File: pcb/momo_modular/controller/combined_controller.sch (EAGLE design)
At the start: 48 parts, among them Q2 P-MOSFET, U1 XRP7659, U2 PIC24FJ64GA306, U3 MCP1702, U5 FLASH8MSOP8, U6 MCP73811

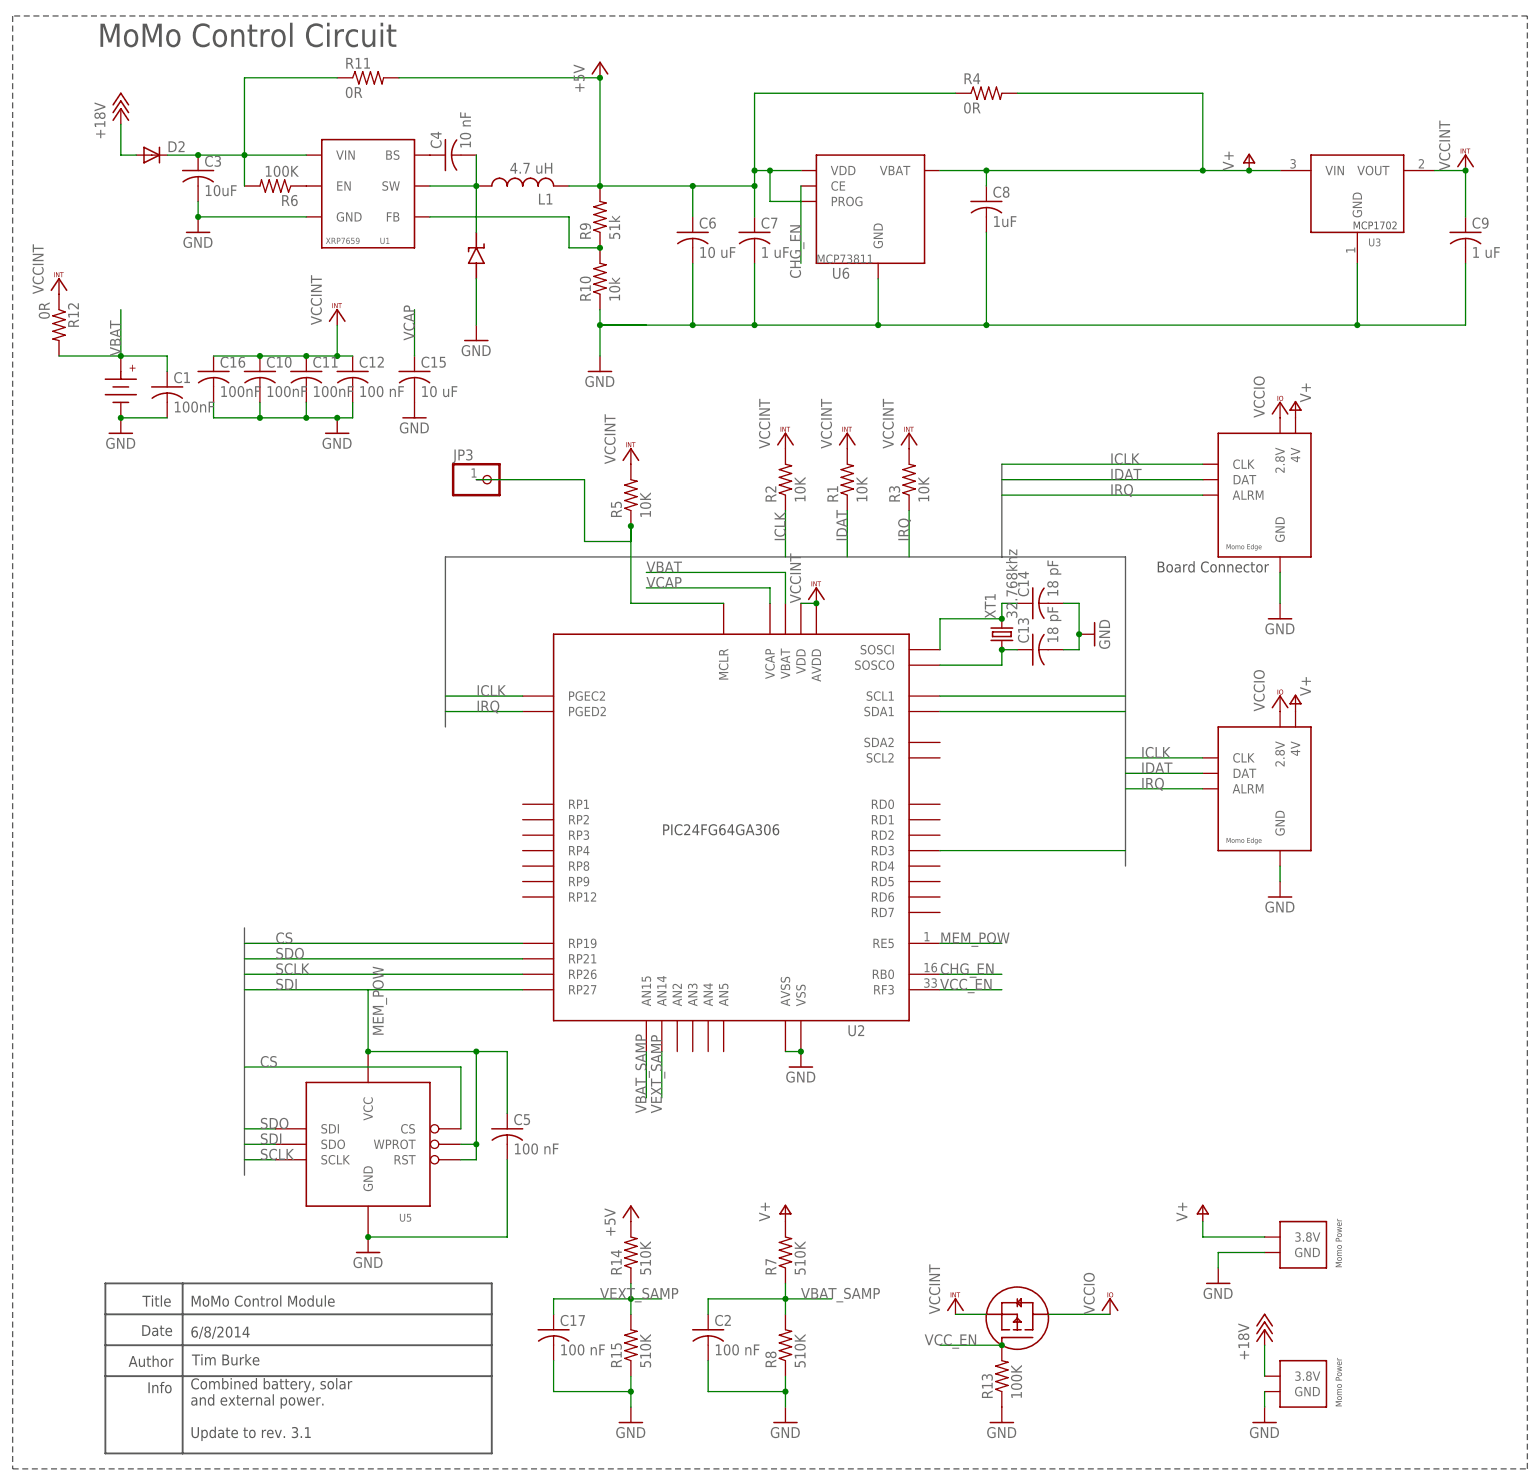
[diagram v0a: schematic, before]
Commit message: Update pcb build system and bugfixes
- support finding eagle via path
- support automatic creation of Diode Descriptions

Update controller board to rev 4.0.

- New version contains BTLE via Microchip RN4020 module
- Voltage supervisor with hard reset capability from bluetooth
or via microcontroller
- Current monitor for solar and external charging current
- Move 2.8V linear regulator and add RF filtering caps to fix RF
interference problems on GSM transmission.

Rename combined_controller to controller

We don't have different assembly variants anymore so the
combined isn't needed.
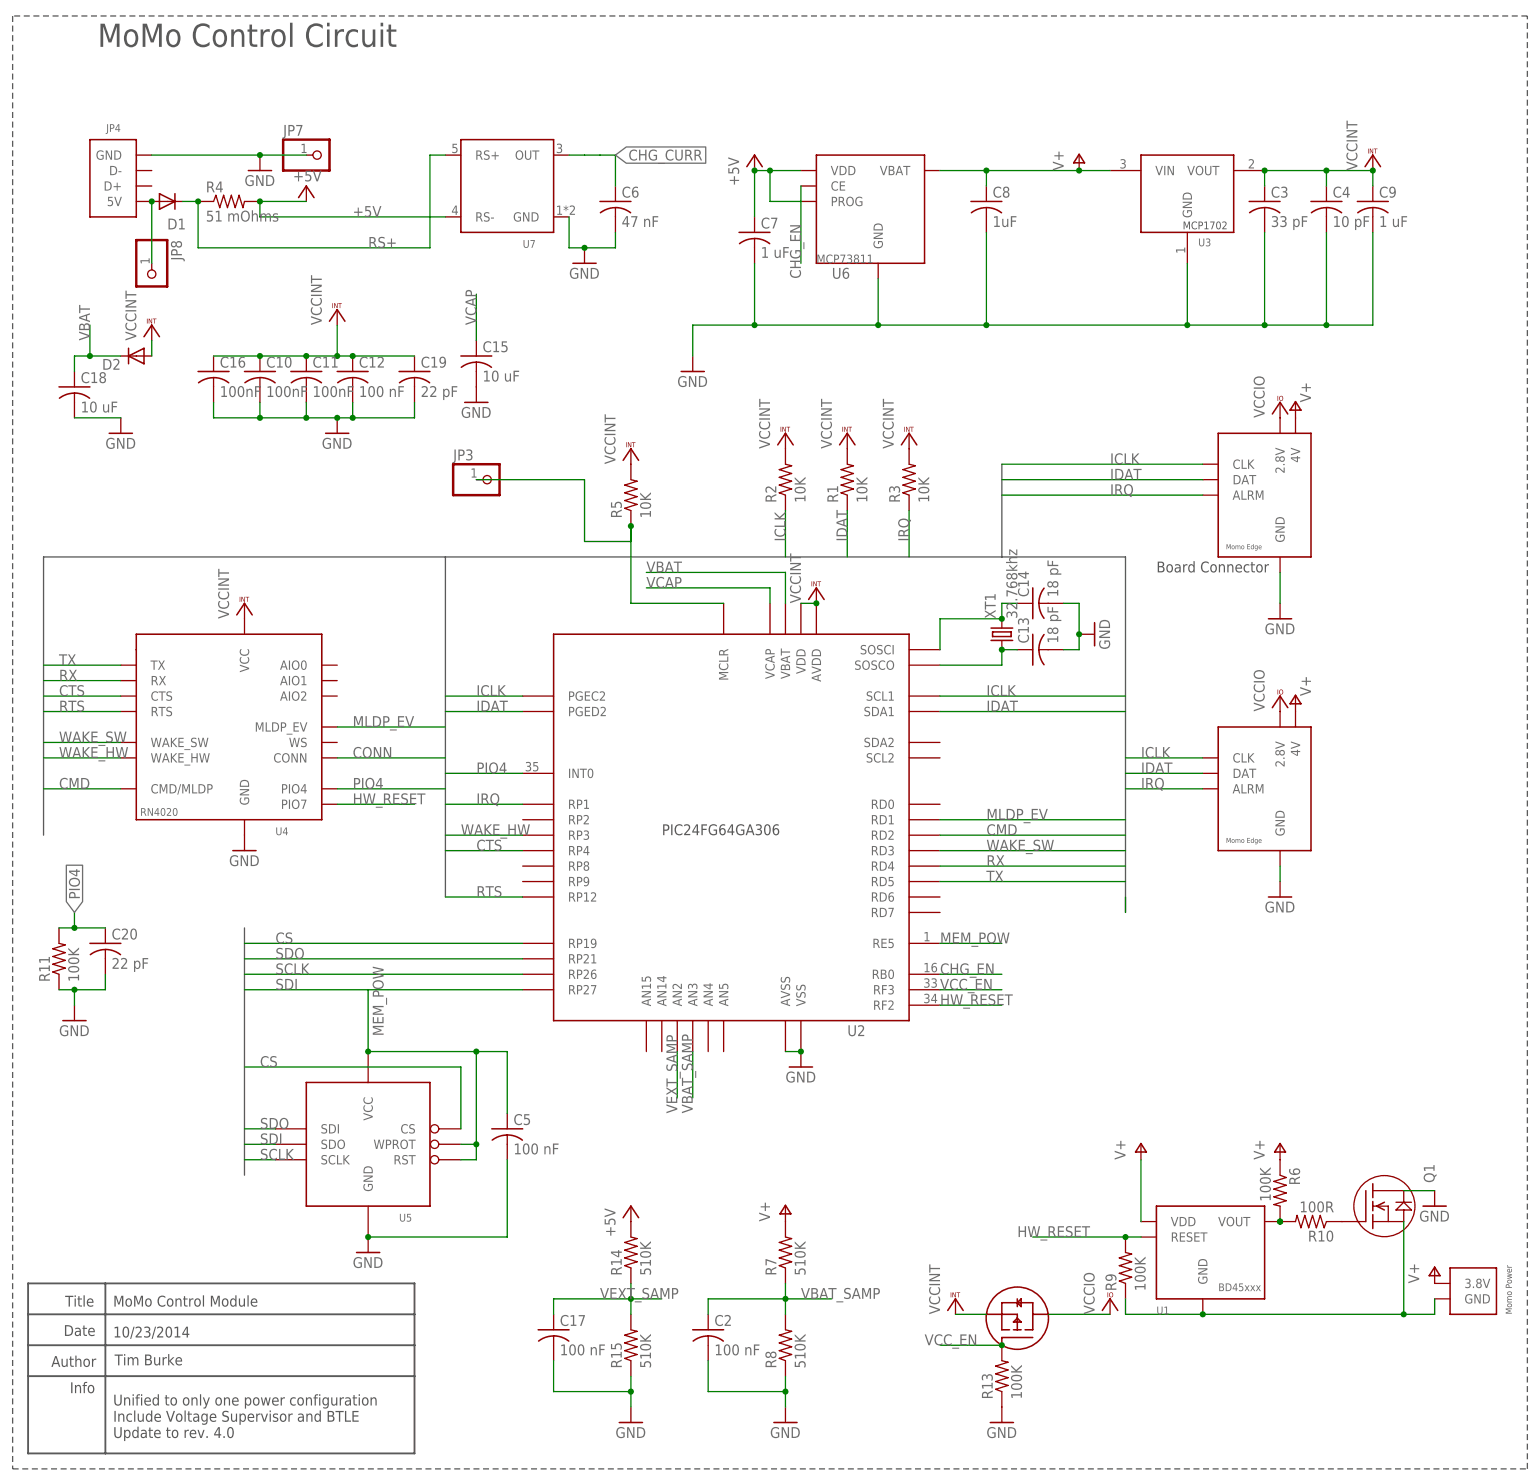
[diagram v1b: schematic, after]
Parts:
- removed BATT1: CR1025-HOLDER, components:CR1025-HOLDER
- removed C1: 100nF, rcl:C-USC0402
- removed L1: 4.7 uH, components:NR6028-INDUCTOR
- removed R12: 0R, rcl:R-US_R0603
- added C18: 10 uF, rcl:C-USC0805K
- added C19, C20: 22 pF, rcl:C-USC0402K
- added JP7, JP8: (no value), pinhead:PINHD-1X1
- added Q1: MOSFET-N, custom_ics:MOSFET-N
- added U4: RN4020_BT_4.0_MODULE, custom_ics:RN4020_BT_4.0_MODULE
- added U7: TS1102-CURRENT-SENSE, custom_ics:TS1102-CURRENT-SENSE
- C10, C11, C12, C16, C17, C2, C5, C9: device rcl:C-USC0402 -> rcl:C-USC0402K
- C15: device rcl:C-USC0805 -> rcl:C-USC0805K
- C3: value 10uF -> 33 pF; device rcl:C-USC0805 -> rcl:C-USC0402K; DIGIKEY-PN (none) -> 1276-1272-1-ND; DIGIKEY-PN-BATT 587-2985-1-ND -> (none); DIGIKEY-PN-EXTPOWER 587-2985-1-ND -> (none)
- C4: value 10 nF -> 10 pF; device rcl:C-USC0402 -> rcl:C-USC0402K; DIGIKEY-PN (none) -> 1276-1139-1-ND; DIGIKEY-PN-BATT 445-1260-1-ND -> (none); DIGIKEY-PN-EXTPOWER 445-1260-1-ND -> (none)
- C6: value 10 uF -> 47 nF; device rcl:C-USC0805 -> rcl:C-USC0402K; DIGIKEY-PN (none) -> 1276-1573-1-ND; DIGIKEY-PN-BATT 587-2985-1-ND -> (none); DIGIKEY-PN-EXTPOWER 587-2985-1-ND -> (none)
- C7, C8: device rcl:C-USC0402 -> rcl:C-USC0402K; DIGIKEY-PN (none) -> 445-4114-1-ND; DIGIKEY-PN-BATT 445-4114-1-ND -> (none); DIGIKEY-PN-SOLAR 445-4114-1-ND -> (none)
- D1: value DIODE_SS2P3SS2P3 -> (none); device components:DIODE_SS2P3SS2P3 -> diode:DIODE-SC79_INFINEON; DIGIKEY-PN-BATT SS2P3-M3/84AGICT-ND -> (none); DIGIKEY-PN-EXTPOWER SS2P3-M3/84AGICT-ND -> (none)
- D2: device diode:DIODE-DO214AC -> diode:DIODE-SC79_INFINEON; DESCRIPTION Schottky Diode -> (none); DIGIKEY-PN SL13HE3/61TGICT-ND -> (none)
- JP4: value MOMO-PWR-HOUSED -> CONN-MICROUSB-B-RCPT; device components:MOMO-PWR-HOUSED -> custom_ics:CONN-MICROUSB-B-RCPT
- R10: value 10k -> 100R; DIGIKEY-PN (none) -> RHM100CFCT-ND; DIGIKEY-PN-BATT P10.0KHCT-ND -> (none); DIGIKEY-PN-EXTPOWER P13.0KHCT-ND -> (none)
- R11: value 0R -> 100K; DIGIKEY-PN (none) -> P100KHCT-ND; DIGIKEY-PN-SOLAR P0.0GCT-ND -> (none)
- R4: value 0R -> 51 mOhms; device rcl:R-US_R0603 -> rcl:R-US_R0805; DIGIKEY-PN (none) -> RHM.051NCT-ND; DIGIKEY-PN-EXTPOWER P0.0GCT-ND -> (none)
- R6: DIGIKEY-PN (none) -> P100KHCT-ND; DIGIKEY-PN-BATT P100KHCT-ND -> (none); DIGIKEY-PN-EXTPOWER P100KHCT-ND -> (none)
- R9: value 51k -> 100K; DIGIKEY-PN (none) -> P100KHCT-ND; DIGIKEY-PN-BATT P51.0KHCT-ND -> (none); DIGIKEY-PN-EXTPOWER P51.0KHCT-ND -> (none)
- U1: value XRP7659 -> VOLTAGE-SUPERVISOR-BD45312; device components:XRP7659 -> custom_ics:VOLTAGE-SUPERVISOR-BD45312; DIGIKEY-PN-BATT 1016-1751-1-ND -> (none); DIGIKEY-PN-EXTPOWER 1016-1751-1-ND -> (none)
- U6: DIGIKEY-PN-BATT MCP73811T-420I/OTCT-ND -> (none); DIGIKEY-PN-SOLAR MCP73811T-420I/OTCT-ND -> (none); FOOTPRINT (none) -> SOT23-5
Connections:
- removed net +18V: D2.A, JP4.3.8V
- removed net BUCK_EN: R6.1, U1.EN
- removed net N$10: R10.2, R9.1, U1.FB
- removed net N$12: C4.1, U1.BS
- removed net N$13: C4.2, D1.CATH, L1.1, U1.SW
- new net CHG_CURR: C6.1, U7.OUT
- new net CMD: U2.RD2, U4.CMD/MLDP
- new net CONN: U4.CONN
- new net CTS: U2.RP4, U4.CTS
- new net HW_RESET: R9.2, U1.RESET, U2.RF2, U4.PIO7
- new net MLDP_EV: U2.RD1, U4.MLDP_EV
- new net N$5: JP5.GND, Q1.S, R9.1, U1.GND
- new net N$8: R10.2, R6.2, U1.VOUT
- new net N$9: D1.A, JP4.5V, JP8.1
- new net PIO4: C20.1, R11.2, U2.INT0, U4.PIO4
- new net RS+: D1.C, R4.1, U7.RS+
- new net RTS: U2.RP12, U4.RTS
- new net RX: U2.RD4, U4.RX
- new net TX: U2.RD5, U4.TX
- new net WAKE_HW: U2.RP3, U4.WAKE_HW
- new net WAKE_SW: U2.RD3, U4.WAKE_SW
- net +5V: now also R4.2, U7.RS-; no longer C6.1, L1.2, R11.2, R4.1, R9.2
- net GND: now also C18.2, C19.2, C20.2, C4.2, JP7.1, Q1.D, R11.1, U4.GND, U7.GND; no longer BATT1.-, C1.2, D1.AN, JP5.GND, R10.1, U1.GND
- net IDAT: now also U2.PGED2
- net IRQ: now also U2.RP1; no longer U2.PGED2, U2.RD3
- net N$1: now also Q1.G, R10.1; no longer C3.1, D2.C, R11.1, R6.2, U1.VIN
- net V+: now also R6.1, U1.VDD; no longer R4.2
- net VBAT: now also C18.1, D2.C; no longer BATT1.+, C1.1, R12.2
- net VBAT_SAMP: now also U2.AN3; no longer U2.AN15
- net VCCINT: now also C19.1, C3.1, C4.1, D2.A, U4.VCC; no longer R12.1
- net VEXT_SAMP: now also U2.AN2; no longer U2.AN14
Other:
- note added: "10/23/2014"
- note added: "Unified to only one power configuration Include Voltage Supervisor and BTLE Update to rev. 4.0"
- note removed: "6/8/2014"
- note removed: "Combined battery, solar and external power. Update to rev. 3.1"
- moved on the sheet: C15, C3, C4, C6, C9, D2, R10, R11, R4, R6, R9, U3
